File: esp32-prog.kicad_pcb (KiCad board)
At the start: 2 copper layers, 55 x 30 mm, 44 parts, among them J1 USB_B_Micro_10118194-0001LF, J2 1.27mm_50mils_male_DW127R-22-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, Q1 AO3400A, Q2 AO3400A, SW1 SW_DIP_x02_50mil_1.27mm_TP-02, U1 AMS1117-3.3, U2 SRV05-4, U3 CH340C, U4 74LVC1G125GW_Nexperia, U5 74LVC1G125GW_Nexperia, U6 74LVC1G125GW_Nexperia, U7 74LVC1G125GW_Nexperia

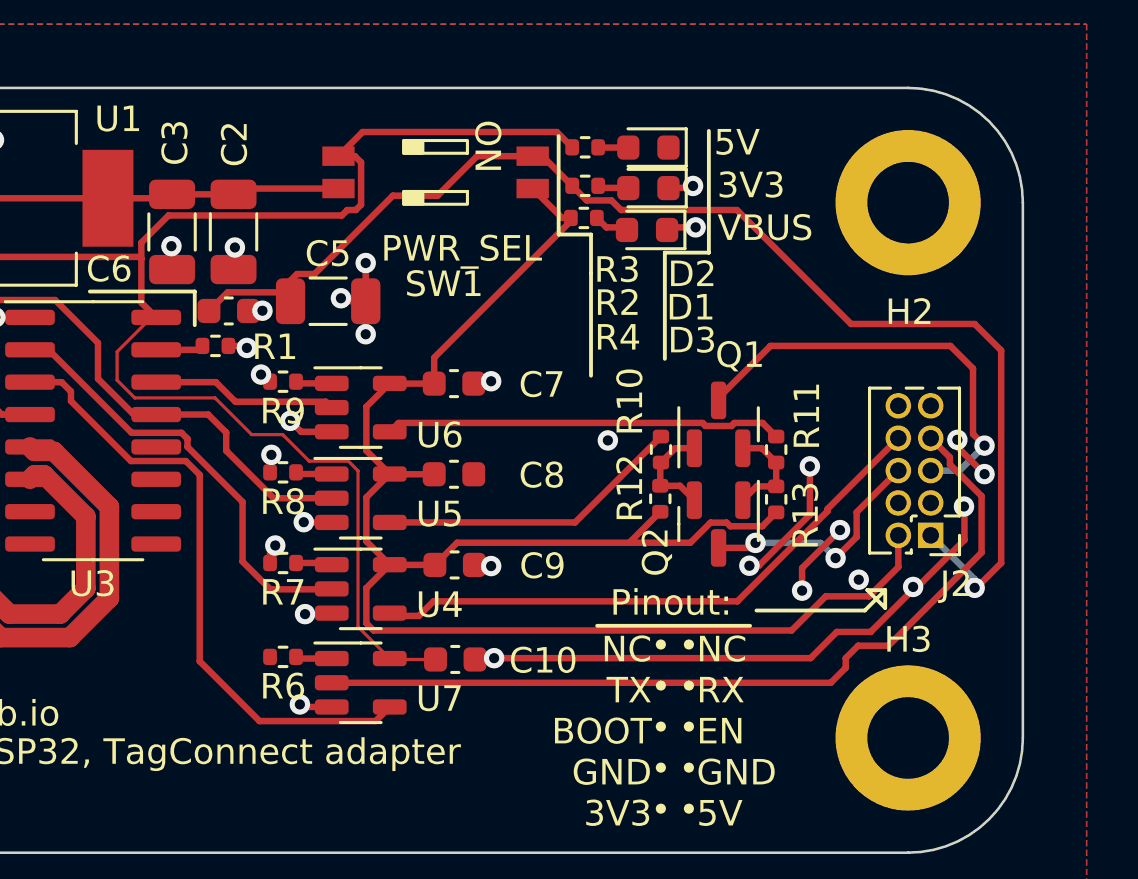
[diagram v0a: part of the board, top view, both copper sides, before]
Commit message: fab: fix 4.7u cap and buffer FP
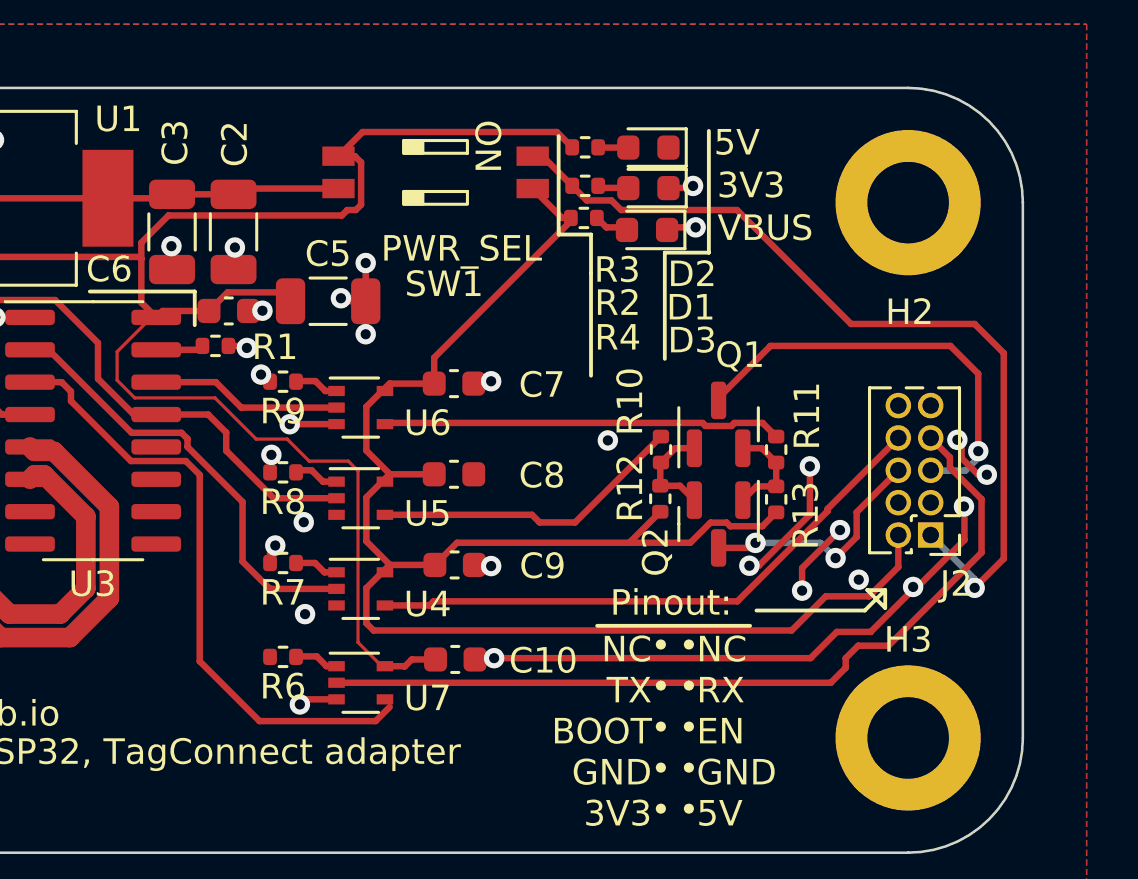
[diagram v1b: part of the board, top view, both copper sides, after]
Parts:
- C2, C3, C5: value 22u_1206_CL31A226KPHNNNE -> 4.7u_1206_1206B475K500NT
- U4, U5, U6, U7: footprint Package_TO_SOT_SMD:SOT-23-5 -> Package_TO_SOT_SMD:SOT-353_SC-70-5
- moved J2 2.63 mm to (200.8, 62.5)
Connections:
- C5 pad 1: +5V -> VBUS
- C6 pad 1: +5V -> VBUS
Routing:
- net +5V: track 49.2 -> 33.7 mm
- net VBUS: track 64.9 -> 70.8 mm

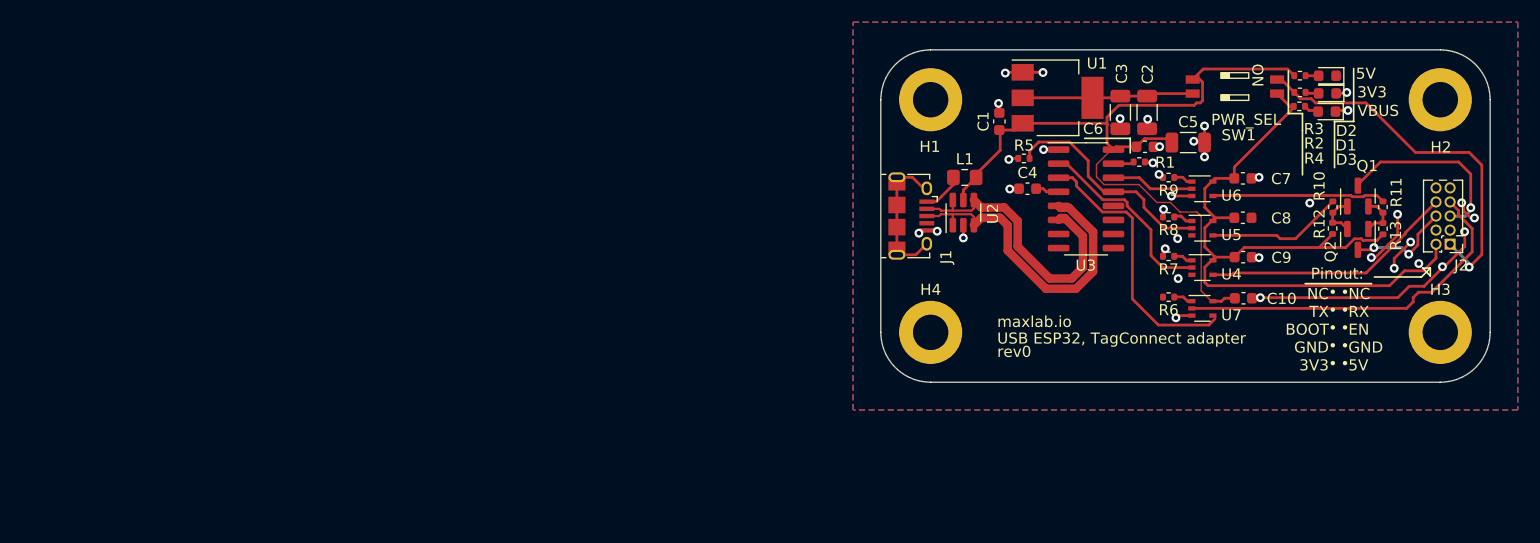
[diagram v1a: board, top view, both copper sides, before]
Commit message: pcb: next revision schematics and prelim routing
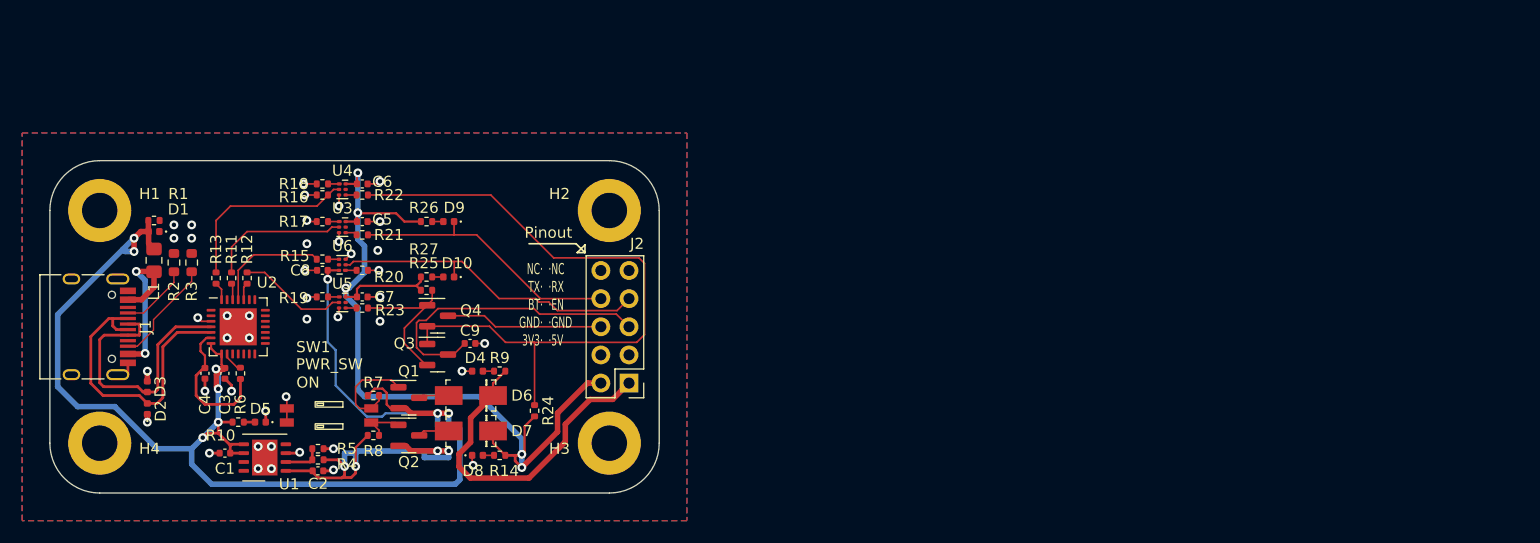
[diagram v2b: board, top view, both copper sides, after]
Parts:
- removed the C5 at (177.7, 55.9)
- removed the C6 at (173.8, 56.2)
- removed the R10 at (190.8, 61.7)
- removed U7: 74LVC1G125GW_Nexperia, Package_TO_SOT_SMD:SOT-353_SC-70-5
- added C9: 10u_0402_LDK105CBJ106MVLF, Capacitor_SMD:C_0402_1005Metric, F.Cu at (112.9, 74.0)
- added D1: SOD-882_0402_RCLAMP0521P-N, Diode_SMD:D_0402_1005Metric, F.Cu at (84.4, 63.9)
- added D10: 0402_BLUE_NCD0402B1, LED_SMD:LED_0402_1005Metric, F.Cu at (111.0, 68.0)
- added D2: SOD-882_0402_RCLAMP0521P-N, Diode_SMD:D_0402_1005Metric, F.Cu at (83.8, 79.9)
- added D3: SOD-882_0402_RCLAMP0521P-N, Diode_SMD:D_0402_1005Metric, F.Cu at (83.8, 77.9)
- added D6: SS34, 00-kiml-diode:DO-214AC, F.Cu at (113.0, 78.7)
- added D7: SS34, 00-kiml-diode:DO-214AC, F.Cu at (113.0, 81.9)
- added D9: 0402_BLUE_NCD0402B1, LED_SMD:LED_0402_1005Metric, F.Cu at (111.0, 63.0)
- added Q1: AO3401A, Package_TO_SOT_SMD:SOT-23, F.Cu at (107.4, 78.9)
- added Q2: AO3401A, Package_TO_SOT_SMD:SOT-23, F.Cu at (107.4, 82.3)
- added R12: 32.4R_0402_AC0402FR-0732R4L, Resistor_SMD:R_0402_1005Metric, F.Cu at (92.8, 68.1)
- added R13: 32.4R_0402_AC0402FR-0732R4L, Resistor_SMD:R_0402_1005Metric, F.Cu at (90.0, 68.1)
- added R15: 32.4R_0402_AC0402FR-0732R4L, Resistor_SMD:R_0402_1005Metric, F.Cu at (99.6, 66.4)
- added R2: 5.1k_0603_0603WAF5101T5E, Resistor_SMD:R_0603_1608Metric, F.Cu at (86.2, 66.7)
- added R21: 32.4R_0402_AC0402FR-0732R4L, Resistor_SMD:R_0402_1005Metric, F.Cu at (103.2, 64.2)
- added R22: 32.4R_0402_AC0402FR-0732R4L, Resistor_SMD:R_0402_1005Metric, F.Cu at (103.2, 60.6)
- added R23: 32.4R_0402_AC0402FR-0732R4L, Resistor_SMD:R_0402_1005Metric, F.Cu at (103.2, 70.8)
- added R26: 1k_0402_0402WGF1001TCE, Resistor_SMD:R_0402_1005Metric, F.Cu at (109.0, 63.0)
- added R27: 1k_0402_0402WGF1001TCE, Resistor_SMD:R_0402_1005Metric, F.Cu at (109.0, 68.0)
- added R3: 5.1k_0603_0603WAF5101T5E, Resistor_SMD:R_0603_1608Metric, F.Cu at (87.8, 66.7)
- added R4: 56k_0402_ERJ2RKF5602X, Resistor_SMD:R_0402_1005Metric, F.Cu at (99.2, 84.5)
- added R5: 10k_0402_0402WGF1002TCE, Resistor_SMD:R_0402_1005Metric, F.Cu at (99.2, 83.5)
- added R6: 10k_0402_0402WGF1002TCE, Resistor_SMD:R_0402_1005Metric, F.Cu at (92.2, 76.7)
- added R7: 10k_0402_0402WGF1002TCE, Resistor_SMD:R_0402_1005Metric, F.Cu at (104.2, 78.7)
- added R8: 10k_0402_0402WGF1002TCE, Resistor_SMD:R_0402_1005Metric, F.Cu at (104.2, 82.3)
- C1: value 100n_0402_CL05B104KB54PNC -> 10u_0402_LDK105CBJ106MVLF; footprint Capacitor_SMD:C_0603_1608Metric -> Capacitor_SMD:C_0402_1005Metric
- C2, C3: value 4.7u_1206_1206B475K500NT -> 10u_0402_LDK105CBJ106MVLF; footprint Capacitor_SMD:C_1206_3216Metric -> Capacitor_SMD:C_0402_1005Metric
- C4: value 10n_0402_CL05B103KB5NNNC -> 10u_0402_LDK105CBJ106MVLF; footprint Capacitor_SMD:C_0603_1608Metric -> Capacitor_SMD:C_0402_1005Metric
- C5: renamed from C7; value 100n_0402_CL05B104KB54PNC -> 10u_0402_LDK105CBJ106MVLF; footprint Capacitor_SMD:C_0603_1608Metric -> Capacitor_SMD:C_0402_1005Metric
- C6: renamed from C8; value 100n_0402_CL05B104KB54PNC -> 10u_0402_LDK105CBJ106MVLF; footprint Capacitor_SMD:C_0603_1608Metric -> Capacitor_SMD:C_0402_1005Metric
- C7: renamed from C9; value 100n_0402_CL05B104KB54PNC -> 10u_0402_LDK105CBJ106MVLF; footprint Capacitor_SMD:C_0603_1608Metric -> Capacitor_SMD:C_0402_1005Metric
- C8: renamed from C10; value 100n_0402_CL05B104KB54PNC -> 10u_0402_LDK105CBJ106MVLF; footprint Capacitor_SMD:C_0603_1608Metric -> Capacitor_SMD:C_0402_1005Metric
- D4: renamed from D1; value 0603_RED_KT-0603R -> 0402_RED_16-213SDRC/S530-A3/TR8; footprint LED_SMD:LED_0603_1608Metric -> LED_SMD:LED_0402_1005Metric
- D5: renamed from D2; value 0603_RED_KT-0603R -> 0402_RED_16-213SDRC/S530-A3/TR8; footprint LED_SMD:LED_0603_1608Metric -> LED_SMD:LED_0402_1005Metric
- D8: renamed from D3; value 0603_RED_KT-0603R -> 0402_RED_16-213SDRC/S530-A3/TR8; footprint LED_SMD:LED_0603_1608Metric -> LED_SMD:LED_0402_1005Metric
- J1: value USB_B_Micro_10118194-0001LF -> TYPE-C-31-M-12; footprint 00-kiml-connector-usb:USB_Micro-B_Amphenol_10118194_Horizontal -> 00-kiml-connector-usb:USB_C_Receptacle_HRO_TYPE-C-31-M-12
- J2: value 1.27mm_50mils_male_DW127R-22-10-23_02x05 -> Conn-02x05_PZ254-2-05-Z-8.5; footprint Connector_PinHeader_1.27mm:PinHeader_2x05_P1.27mm_Vertical -> Connector_PinHeader_2.54mm:PinHeader_2x05_P2.54mm_Vertical
- L1: value 0805_FB_220R@100MHz_BLM21PG221SN1D -> FB_2A_0805_220R@100MHz_BLM21PG221SN1D
- R11: value 1k_0402_0402WGF1001TCE -> 32.4R_0402_AC0402FR-0732R4L
- SW1: footprint 00-kiml-button-switch-smd:SW_DIP_1.27mm_0.50mil_TP-02 -> 00-kiml-switch-button-smd:SW_DIP_1.27mm_0.50mil_TP-02
- U1: value AMS1117-3.3 -> LD39200DPUR; footprint Package_TO_SOT_SMD:SOT-223-3_TabPin2 -> Package_DFN_QFN:DFN-8-1EP_4x4mm_P0.8mm_EP2.3x3.24mm
- U2: value SRV05-4 -> CP2102-GMR; footprint Package_TO_SOT_SMD:SOT-23-6 -> Package_DFN_QFN:QFN-28-1EP_5x5mm_P0.5mm_EP3.35x3.35mm
- U3: value CH340C -> TI_SN74LVC1G125DRYR; footprint Package_SO:SOIC-16_3.9x9.9mm_P1.27mm -> Package_SON:Texas_USON-6_1x1.45mm_P0.5mm_SMD
- U4, U5, U6: value 74LVC1G125GW_Nexperia -> TI_SN74LVC1G125DRYR; footprint Package_TO_SOT_SMD:SOT-353_SC-70-5 -> Package_SON:Texas_USON-6_1x1.45mm_P0.5mm_SMD
- moved R11 104.1 mm to (91.4, 68.1), turned to 90 degrees
- moved D5 101.3 mm to (94.0, 81.1)
- moved R10 100.8 mm to (92.0, 81.1)
- moved R1 89.1 mm to (84.4, 62.9), turned to 0 degrees
- moved SW1 87.0 mm to (100.2, 80.5)
- moved R25 86.5 mm to (109.0, 69.2), turned to 0 degrees
- moved Q3 84.3 mm to (110.0, 75.0), turned to 0 degrees
- moved C3 84.2 mm to (90.8, 76.7)
- moved Q4 83.3 mm to (110.0, 71.5), turned to 0 degrees
- moved C8 83.2 mm to (99.6, 67.4), turned to 180 degrees
- moved D8 82.7 mm to (113.6, 84.1), turned to 0 degrees
- moved C2 81.5 mm to (99.2, 85.5), turned to 180 degrees
- moved D4 80.7 mm to (113.6, 76.5), turned to 0 degrees
- moved C7 79.6 mm to (103.2, 69.8)
- moved C5 79.6 mm to (103.2, 63.0)
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- renumbered Q1 to Q3, Q2 to Q4, R3 to R10, R4 to R14, R5 to R16, R7 to R17, R8 to R18, R9 to R19, R6 to R20, R12 to R24, R13 to R25, R2 to R9
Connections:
- C1 pad 1: VBUS -> GND
- C1 pad 2: GND -> VBUS
- C2 pad 1: +3.3VA -> GND
- C2 pad 2: GND -> +3.3VA
- C3 pad 1: +3.3VA -> VBUS
- C4 pad 1: GND -> Net-(U2-VDD)
- C4 pad 2: Net-(C4-Pad2) -> GND
- L1 pad 1: Net-(J1-Pad1) -> Net-(J1-VBUS-PadA4)
- Q3 pad 2: Net-(Q1-Pad2) -> Net-(Q3-S)
- Q4 pad 1: Net-(Q1-Pad2) -> Net-(Q3-S)
- R1 pad 1: GND -> VBUS
- R1 pad 2: Net-(R1-Pad2) -> GND
- R11 pad 1: Net-(R11-Pad1) -> Net-(U2-TXD)
- R11 pad 2: Net-(Q1-Pad2) -> Net-(R11-Pad2)
- R16 pad 2: Net-(R5-Pad2) -> Net-(R13-Pad2)
- R17 pad 1: Net-(R7-Pad1) -> Net-(R17-Pad1)
- R18 pad 1: Net-(R8-Pad1) -> Net-(R18-Pad1)
- R19 pad 1: Net-(R9-Pad1) -> Net-(R19-Pad1)
- R20 pad 1: Net-(R6-Pad1) -> Net-(R20-Pad1)
- R25 pad 2: Net-(Q1-Pad2) -> Net-(Q3-S)
- SW1 pad 1: VBUS -> GND
- SW1 pad 2: +3.3VA -> GND
- SW1 pad 3: +3.3V -> Net-(Q2-G)
- SW1 pad 4: +5V -> Net-(Q1-G)
- U1 pad 1: GND -> +3.3VA
- U1 pad 2: +3.3VA -> Net-(U1-ADJ)
- U1 pad 3: VBUS -> GND
- U2 pad 1: /UD+ -> unconnected-(U2-~{DCD}-Pad1)
- U2 pad 2: GND -> unconnected-(U2-~{RI}/CLK-Pad2)
- U2 pad 3: /UD+ -> GND
- U2 pad 4: /UD- -> /UD+
- U2 pad 5: VBUS -> /UD-
- U2 pad 6: /UD- -> Net-(U2-VDD)
- U3 pad 1: GND -> Net-(R17-Pad1)
- U3 pad 2: Net-(U3-Pad2) -> Net-(R11-Pad2)
- U3 pad 3: Net-(U3-Pad3) -> GND
- U3 pad 4: Net-(C4-Pad2) -> Net-(R21-Pad1)
- U3 pad 5: /UD+ -> (no net)
- U3 pad 6: /UD- -> +3.3V
- U4 pad 1: Net-(R7-Pad1) -> Net-(R18-Pad1)
- U4 pad 2: Net-(U3-Pad2) -> Net-(R13-Pad2)
- U4 pad 4: /TXD -> Net-(R22-Pad1)
- U4 pad 5: +3.3V -> (no net)
- U5 pad 1: Net-(R8-Pad1) -> Net-(R19-Pad1)
- U5 pad 2: Net-(R5-Pad2) -> Net-(R12-Pad2)
- U5 pad 5: +3.3V -> (no net)
- U6 pad 1: Net-(R9-Pad1) -> Net-(R20-Pad1)
- U6 pad 2: Net-(U3-Pad14) -> /RXD
- U6 pad 4: Net-(R11-Pad1) -> Net-(R15-Pad2)
- U6 pad 5: +3.3V -> (no net)
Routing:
- net Net-(Q3-G): track 4.00 -> 61.7 mm
- net VBUS: track 70.8 -> 127.3 mm, vias 0 -> 9
- net GND: track 58.4 -> 29.6 mm, vias 38 -> 43
- net Net-(U3-Pad3): track 24.4 -> 0.00 mm
- net Net-(R5-Pad2): track 19.8 -> 0.00 mm
- net +3.3VA: track 15.0 -> 32.8 mm, vias 0 -> 4
- net Net-(R13-Pad2): track 0.00 -> 16.9 mm
- net Net-(U3-Pad2): track 16.8 -> 0.00 mm
- net Net-(R11-Pad1): track 15.6 -> 0.00 mm
- net Net-(J1-VBUS-PadA4): track 0.00 -> 15.1 mm, vias 0 -> 2
- net +3.3V: track 66.5 -> 80.6 mm, vias 0 -> 5
- net Net-(Q3-S): track 0.00 -> 14.1 mm
- net Net-(R11-Pad2): track 0.00 -> 12.7 mm
- net Net-(U2-VDD): track 0.00 -> 12.6 mm
- net unconnected-(J1-Pad6): track 11.7 -> 0.00 mm
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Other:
- board text added: "NC· TX· BT· GND· 3V3·"
- board text added: "Pinout"
- board text added: "esp32-prog-${ISSUE_DATE}-${REVISION}"
- board text added: "·NC ·RX ·EN ·GND ·5V"
- board text removed: "3V3"
- board text removed: "5V"
- board text removed: "NC RX EN GND 5V"
- board text removed: "NC TX BOOT GND 3V3"
- board text removed: "Pinout:"
- board text removed: "VBUS"
- board text removed: "rev0"
- board text removed: "• • • • •"

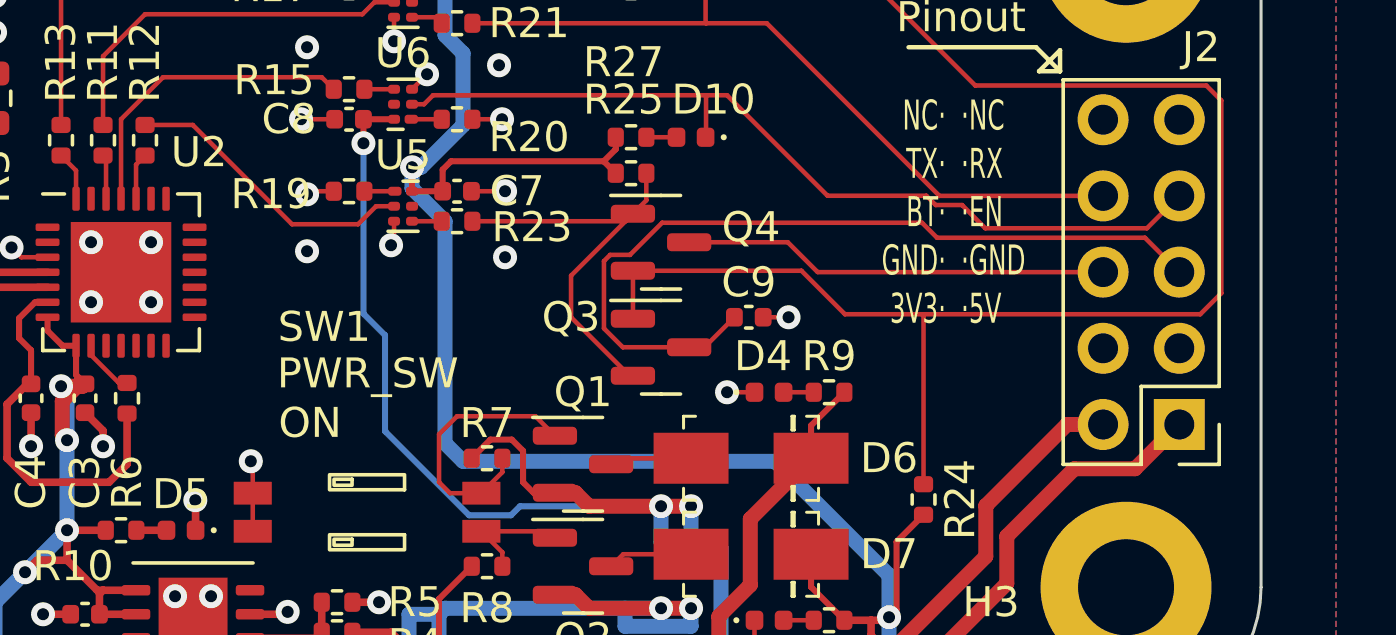
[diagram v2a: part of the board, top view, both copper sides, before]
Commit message: pcb: add markings for the tag connector and pwr switch
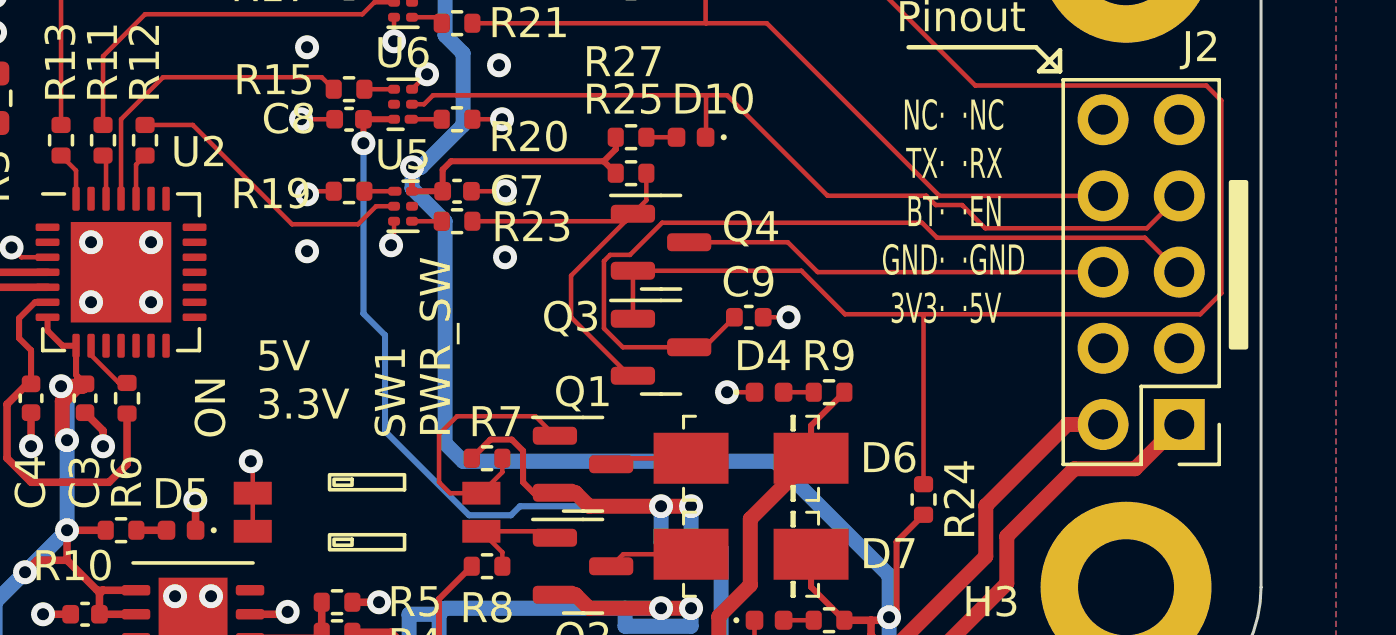
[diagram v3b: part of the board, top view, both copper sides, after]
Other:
- board text added: "5V 3.3V"
